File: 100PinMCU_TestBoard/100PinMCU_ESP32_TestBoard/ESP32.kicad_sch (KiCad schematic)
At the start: 21 parts, among them J1 USB_C_Receptacle_USB2.0_16P, SW1 BOOT Switch, SW2 RESET Button, U1 ESP32-C6-MINI-1

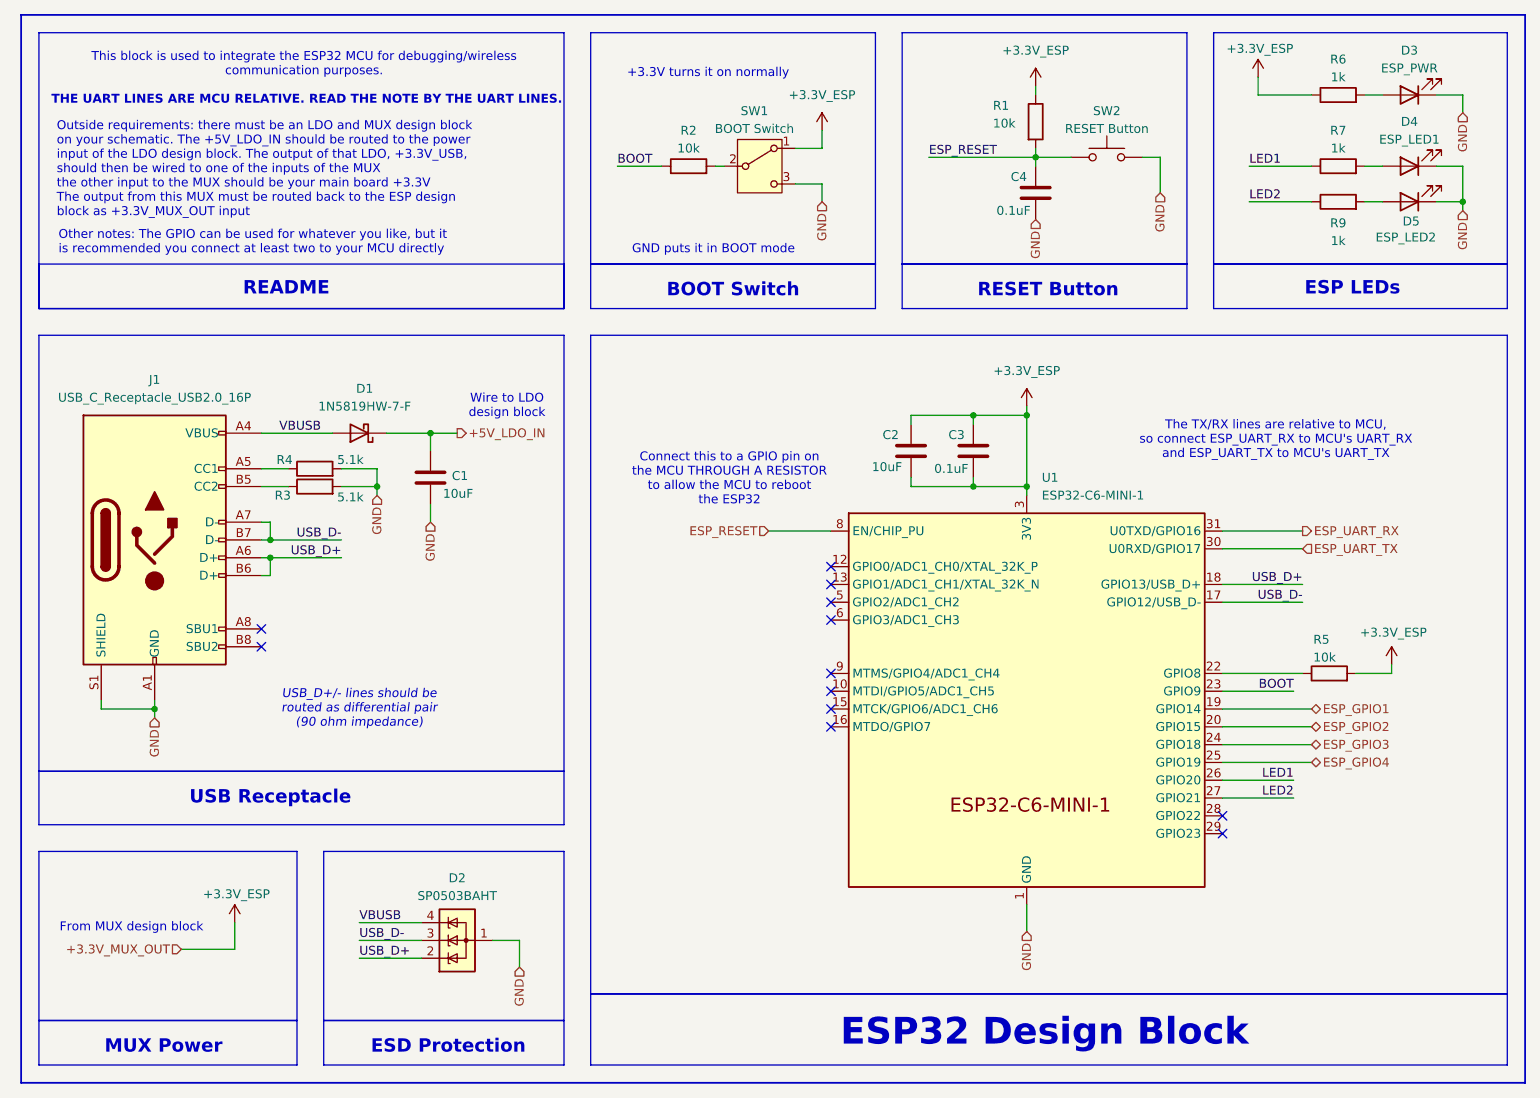
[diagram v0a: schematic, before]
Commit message: esp32 design block will be updated later
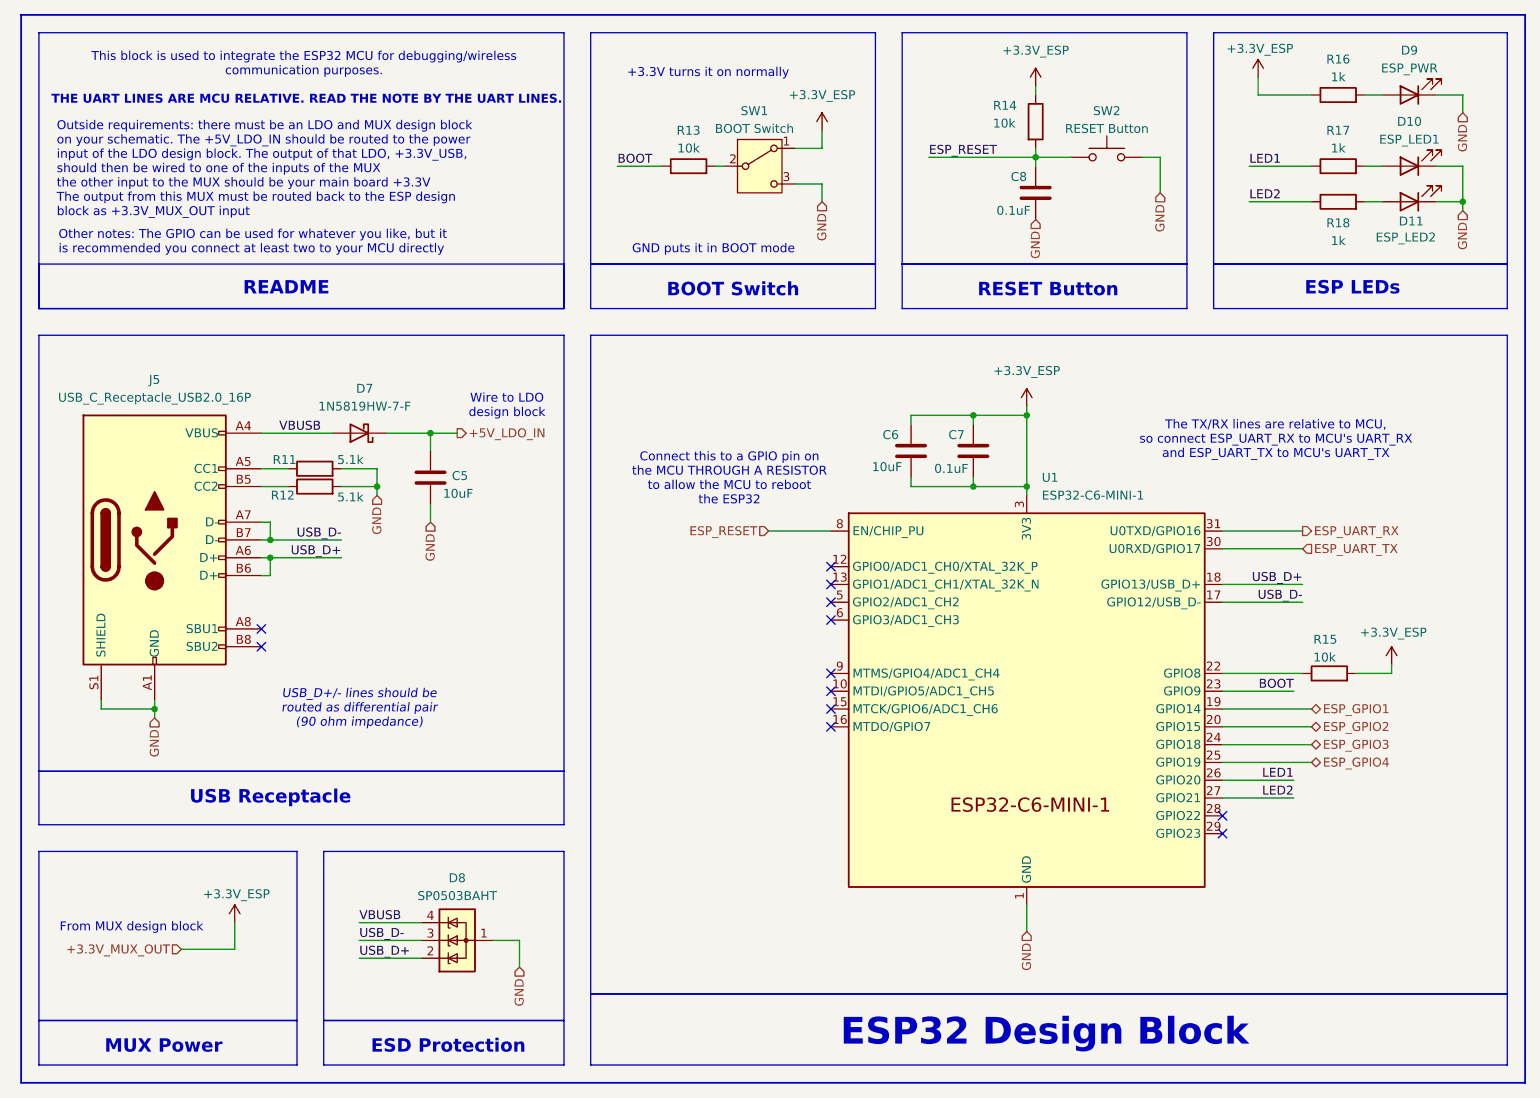
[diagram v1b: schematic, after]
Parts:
- renumbered C1 to C5, C2 to C6, C3 to C7, C4 to C8, D4 to D10, D5 to D11, D1 to D7, D2 to D8, D3 to D9, J1 to J5, R4 to R11, R3 to R12, R2 to R13, R1 to R14, R5 to R15, R6 to R16, R7 to R17, R9 to R18
